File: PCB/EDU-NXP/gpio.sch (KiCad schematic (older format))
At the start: 96 parts, among them P1 CONN_20X2, P2 CONN_20X2

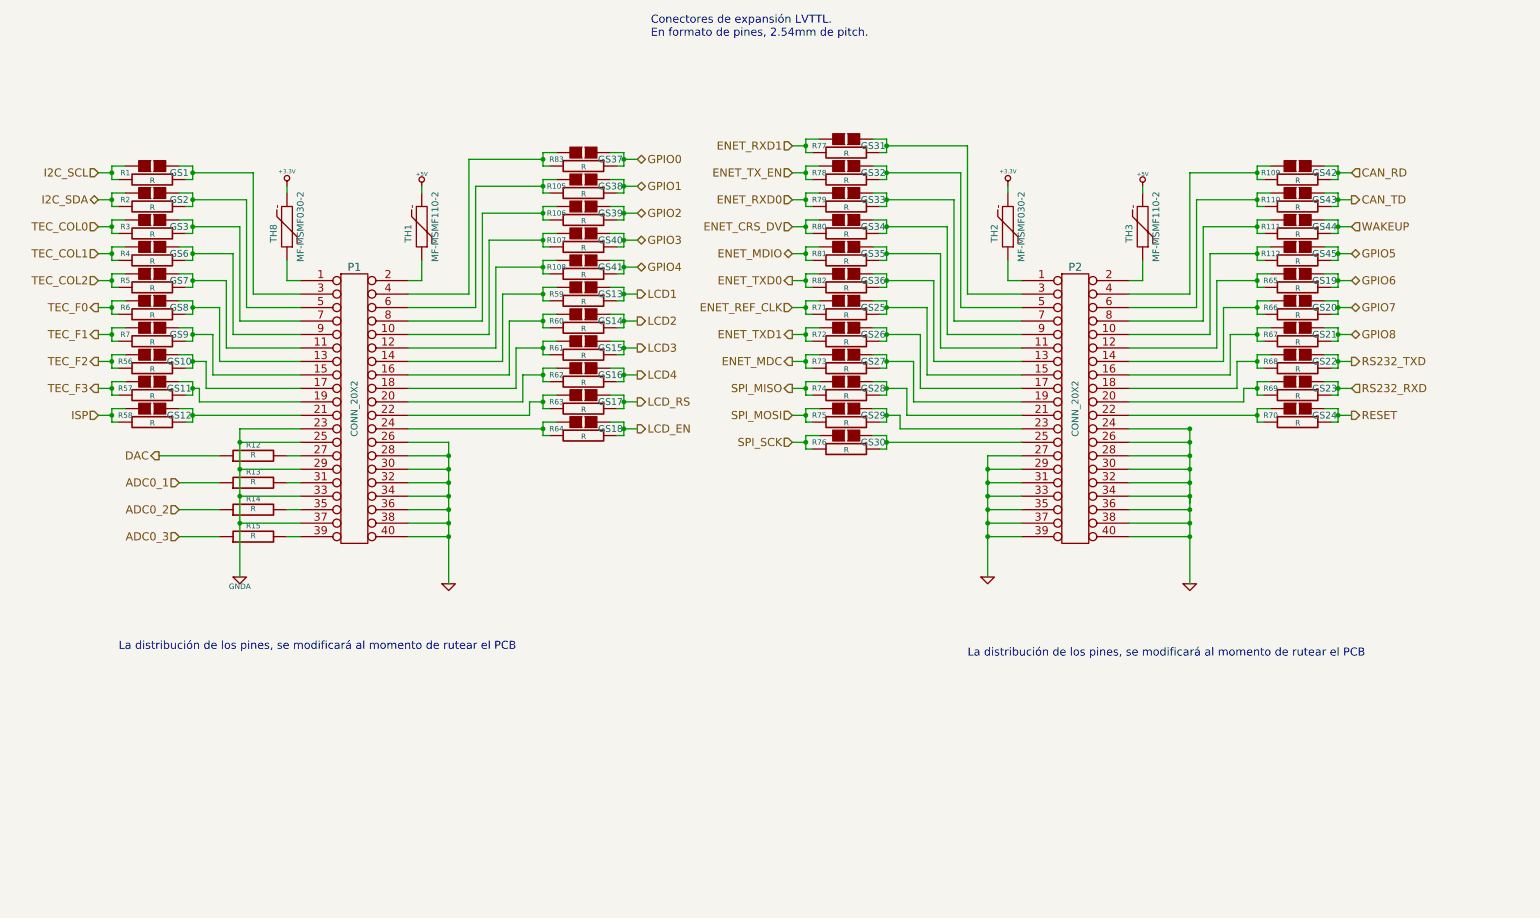
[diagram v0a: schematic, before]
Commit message: Versión completa del esquemático con todos los componentes ya definidos
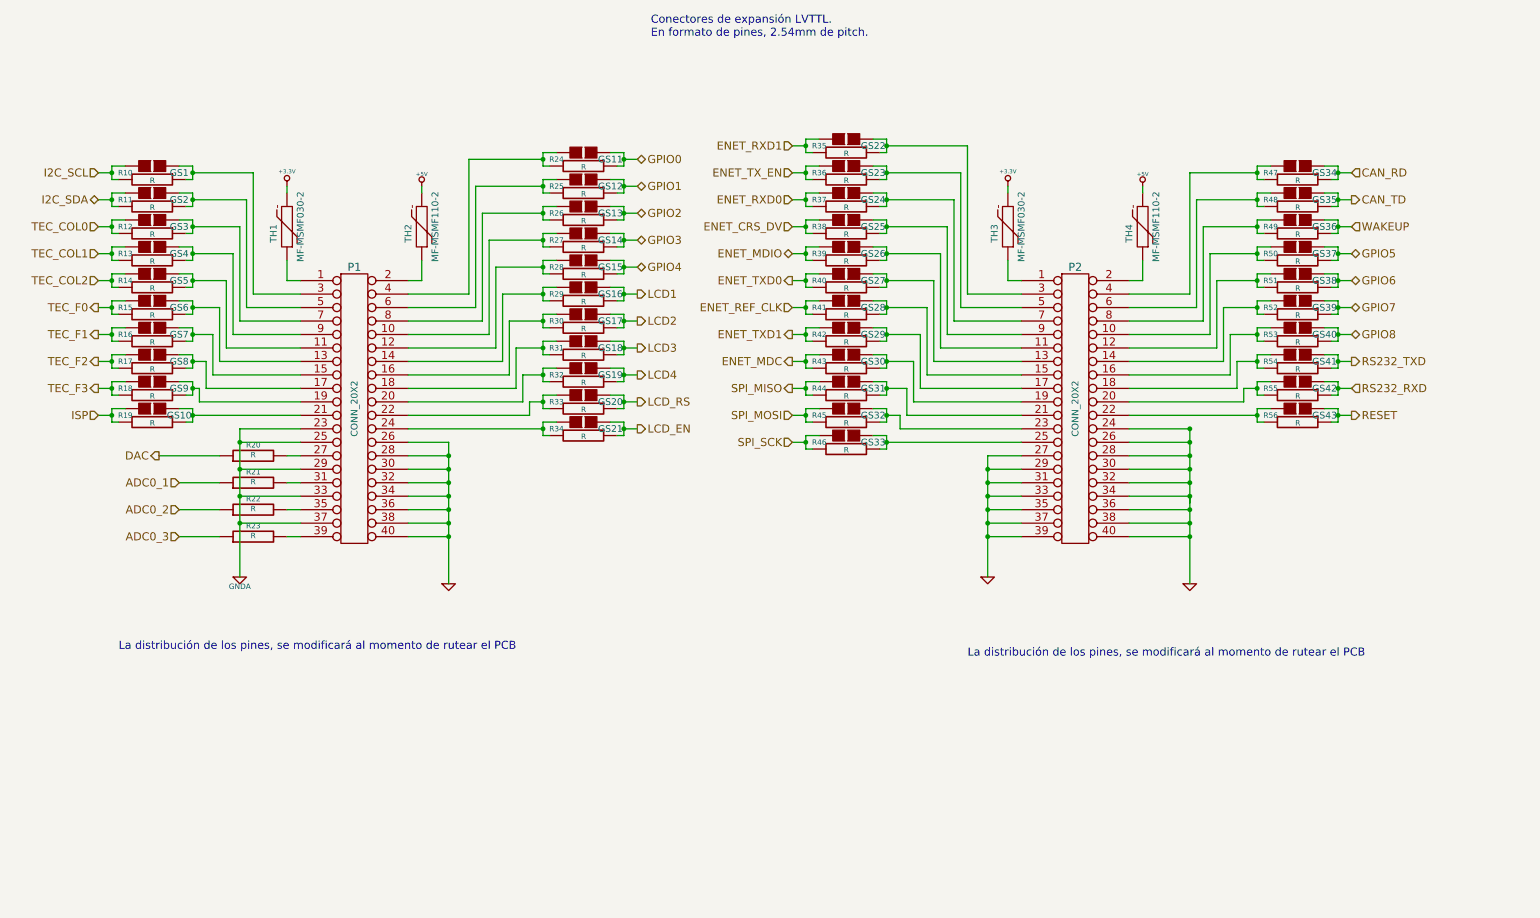
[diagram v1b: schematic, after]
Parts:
- renumbered GS12 to GS10, GS37 to GS11, GS38 to GS12, GS39 to GS13, GS40 to GS14, GS41 to GS15, GS13 to GS16, GS14 to GS17, GS15 to GS18, GS16 to GS19, GS17 to GS20, GS18 to GS21, GS31 to GS22, GS32 to GS23, GS33 to GS24, GS34 to GS25, GS35 to GS26, GS36 to GS27, GS25 to GS28, GS26 to GS29, GS27 to GS30, GS28 to GS31, GS29 to GS32, GS30 to GS33, GS42 to GS34, GS43 to GS35, GS44 to GS36, GS45 to GS37, GS19 to GS38, GS20 to GS39, GS6 to GS4, GS21 to GS40, GS22 to GS41, GS23 to GS42, GS24 to GS43, GS7 to GS5, GS8 to GS6, GS9 to GS7, GS10 to GS8, GS11 to GS9, R1 to R10, R2 to R11, R3 to R12, R4 to R13, R5 to R14, R6 to R15, R7 to R16, R56 to R17, R57 to R18, R58 to R19, R12 to R20, R13 to R21, R14 to R22, R15 to R23, R83 to R24, R105 to R25, R106 to R26, R107 to R27, R108 to R28, R59 to R29, R60 to R30, R61 to R31, R62 to R32, R63 to R33, R64 to R34, R77 to R35, R78 to R36, R79 to R37, R80 to R38, R81 to R39, R82 to R40, R71 to R41, R72 to R42, R73 to R43, R74 to R44, R75 to R45, R76 to R46, R109 to R47, R110 to R48, R111 to R49, R112 to R50, R65 to R51, R66 to R52, R67 to R53, R68 to R54, R69 to R55, R70 to R56, TH8 to TH1, TH1 to TH2, TH2 to TH3, TH3 to TH4

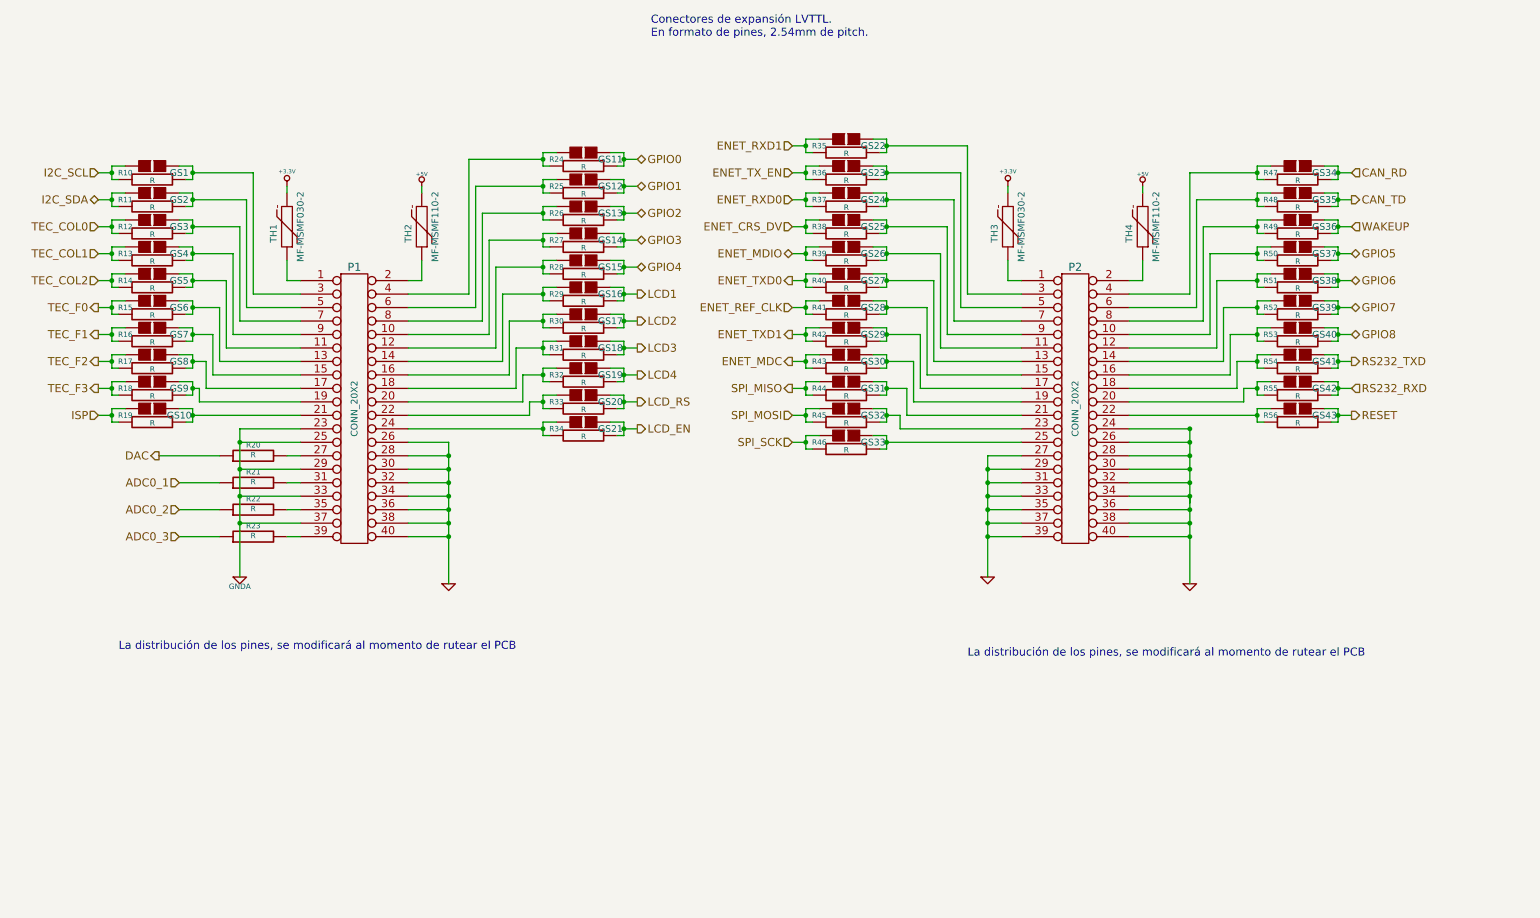
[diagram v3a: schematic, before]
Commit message: Se cambiaron los leds - Avances sobre el ruteo del PCB
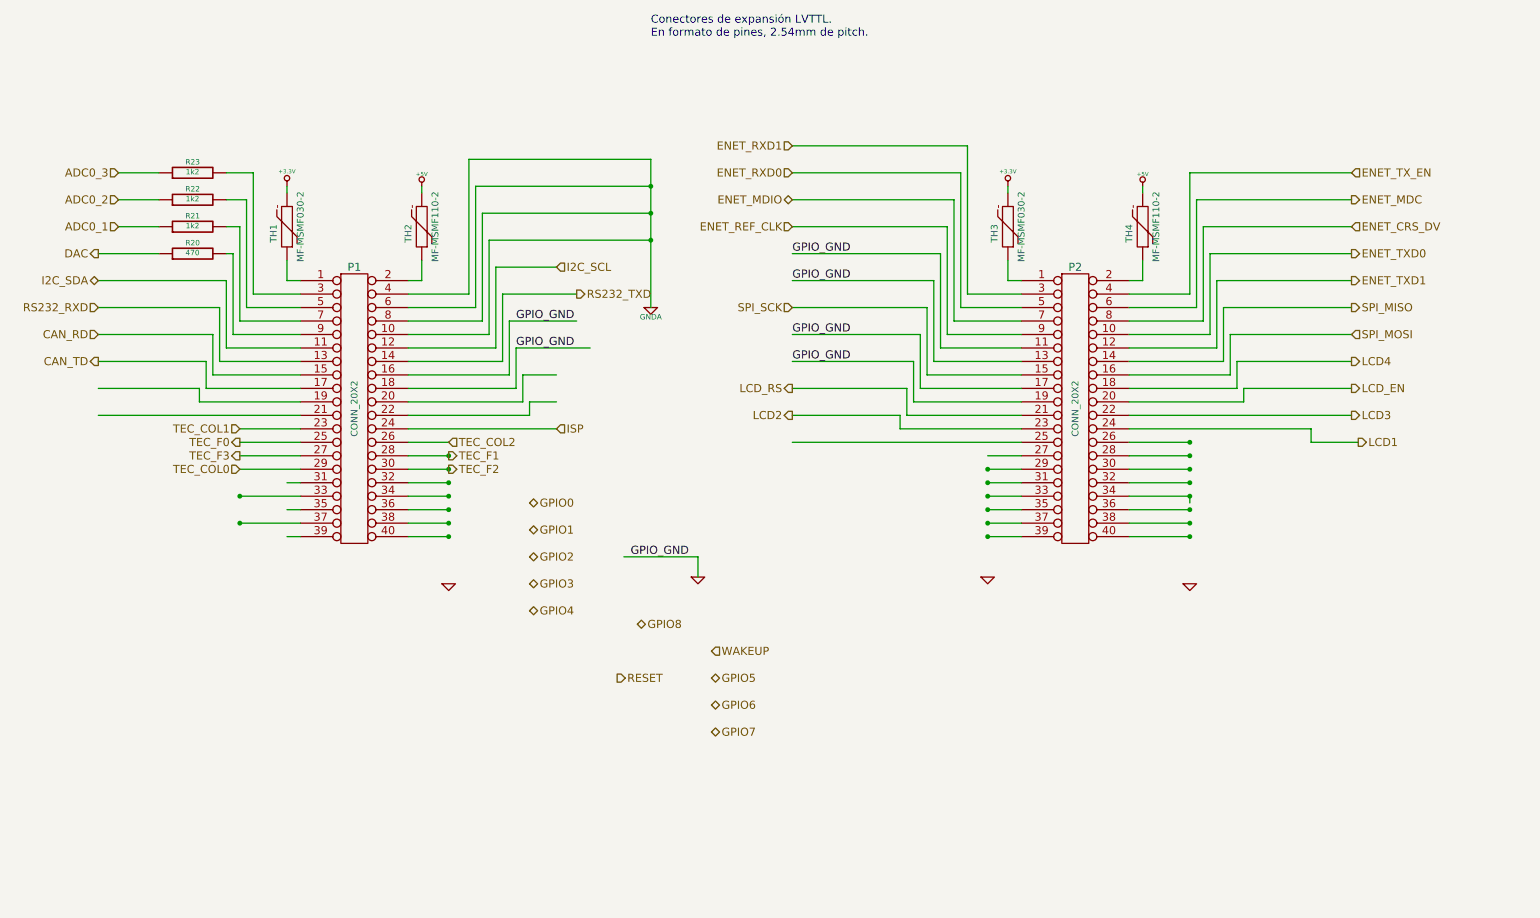
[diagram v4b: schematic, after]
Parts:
- removed GS1, GS10, GS11, GS12, GS13, GS14, GS15, GS16, GS17, GS18, GS19, GS2, GS20, GS21, GS22, GS23, GS24, GS25, GS26, GS27, GS28, GS29, GS3, GS30, GS31, GS32, GS33, GS34, GS35, GS36, GS37, GS38, GS39, GS4, GS40, GS41, GS42, GS43, GS5, GS6, GS7, GS8, GS9: GS2, symbol GS2
- removed R10, R11, R12, R13, R14, R15, R16, R17, R18, R19, R24, R25, R26, R27, R28, R29, R30, R31, R32, R33, R34, R35, R36, R37, R38, R39, R40, R41, R42, R43, R44, R45, R46, R47, R48, R49, R50, R51, R52, R53, R54, R55, R56: R, ~, symbol R
- R20: value R -> 470
- R21, R22, R23: value R -> 1k2
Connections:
- net labels added: GPIO_GND
- wire segments 476 -> 176
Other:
- note removed: "La distribución de los pines, se modificará al momento de rutear el PCB\n"
- moved on the sheet: R20, R21, R22, R23

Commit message: Se completó el ruteo del PCB
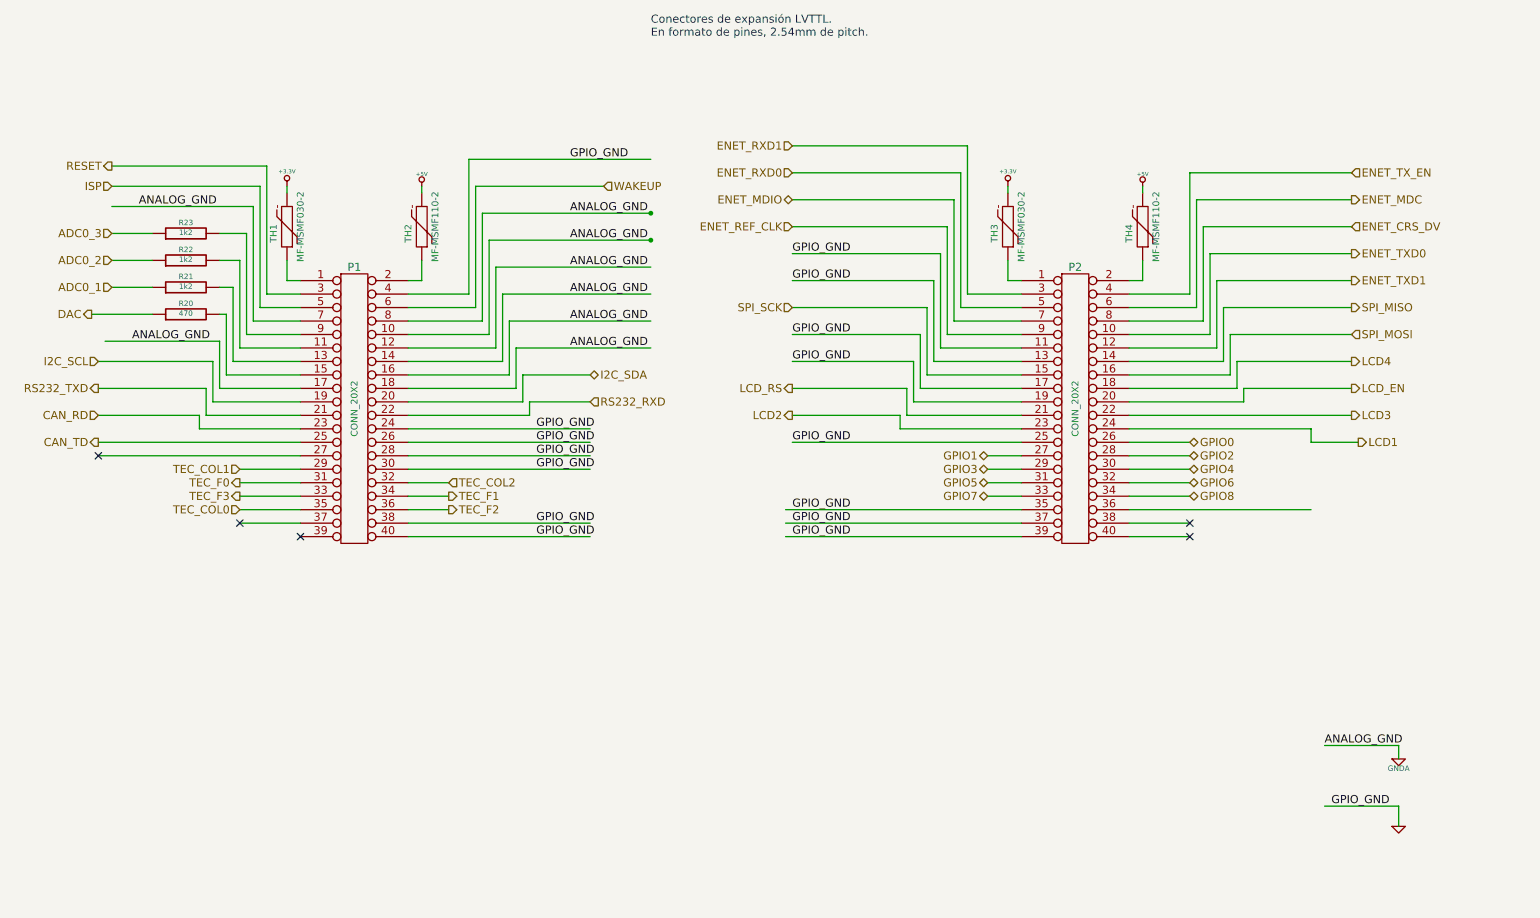
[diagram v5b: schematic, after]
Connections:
- net labels added: ANALOG_GND
- wire segments 176 -> 179
- no-connect marks 0 -> 5
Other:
- moved on the sheet: R20, R21, R22, R23

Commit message: PCB V0.0 finalizado - Se agregaron planos de masa, control de dimensiones y perforaciones, se agregó el LOGO
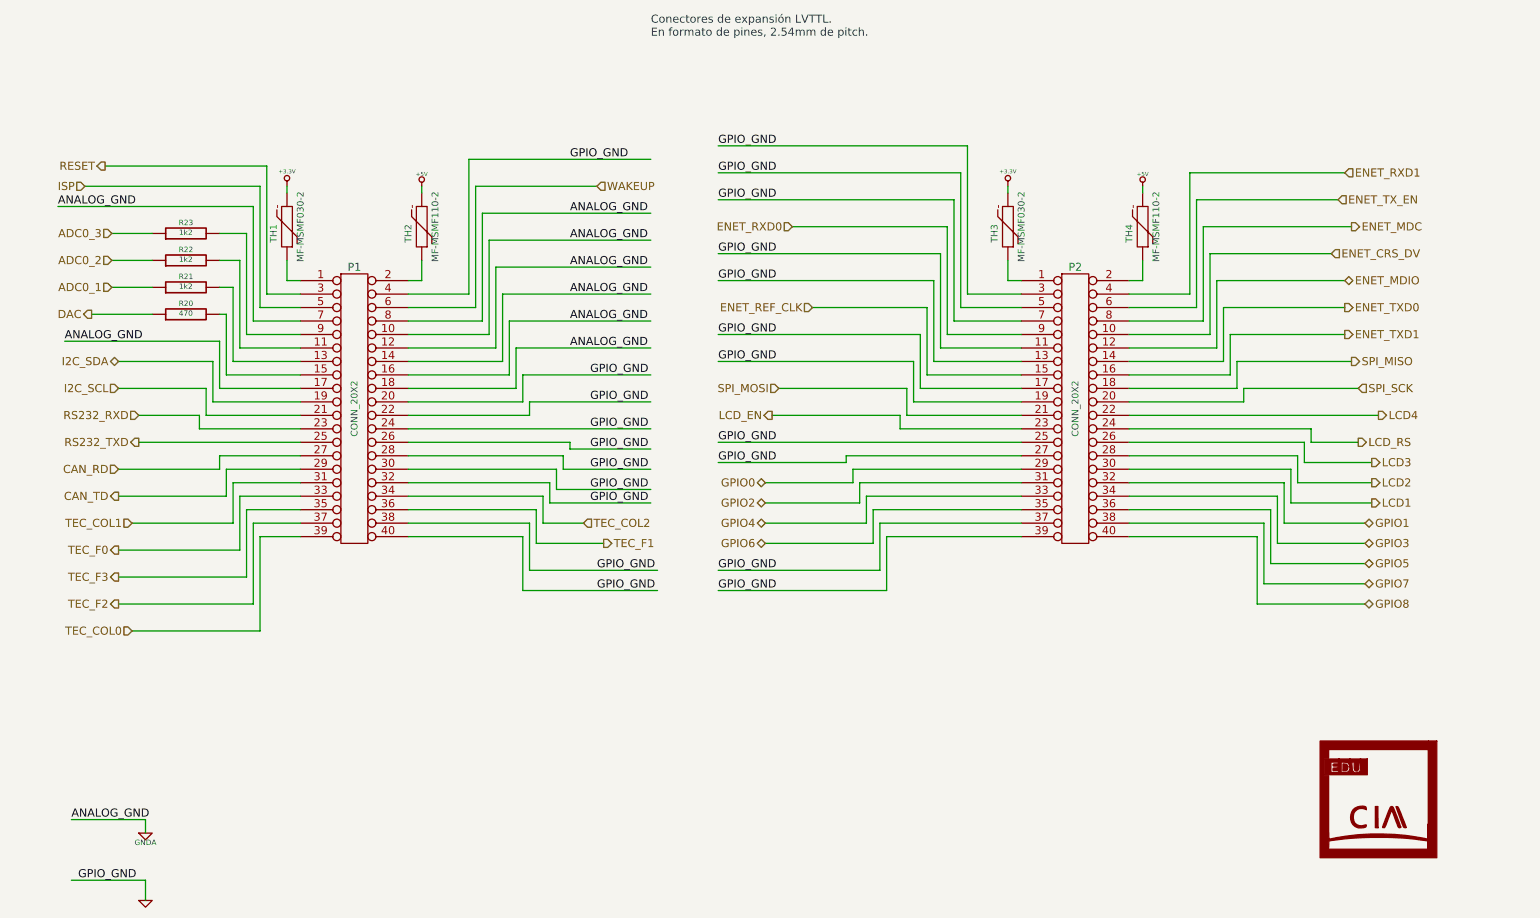
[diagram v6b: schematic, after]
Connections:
- wire segments 179 -> 240
- no-connect marks 5 -> 0
